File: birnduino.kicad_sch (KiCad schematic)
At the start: 28 parts, among them IC1 ATmega328P, IC2 MAX232, Q1 16 MHz, SW1 RESET, U4 78L33, U5 LM7805

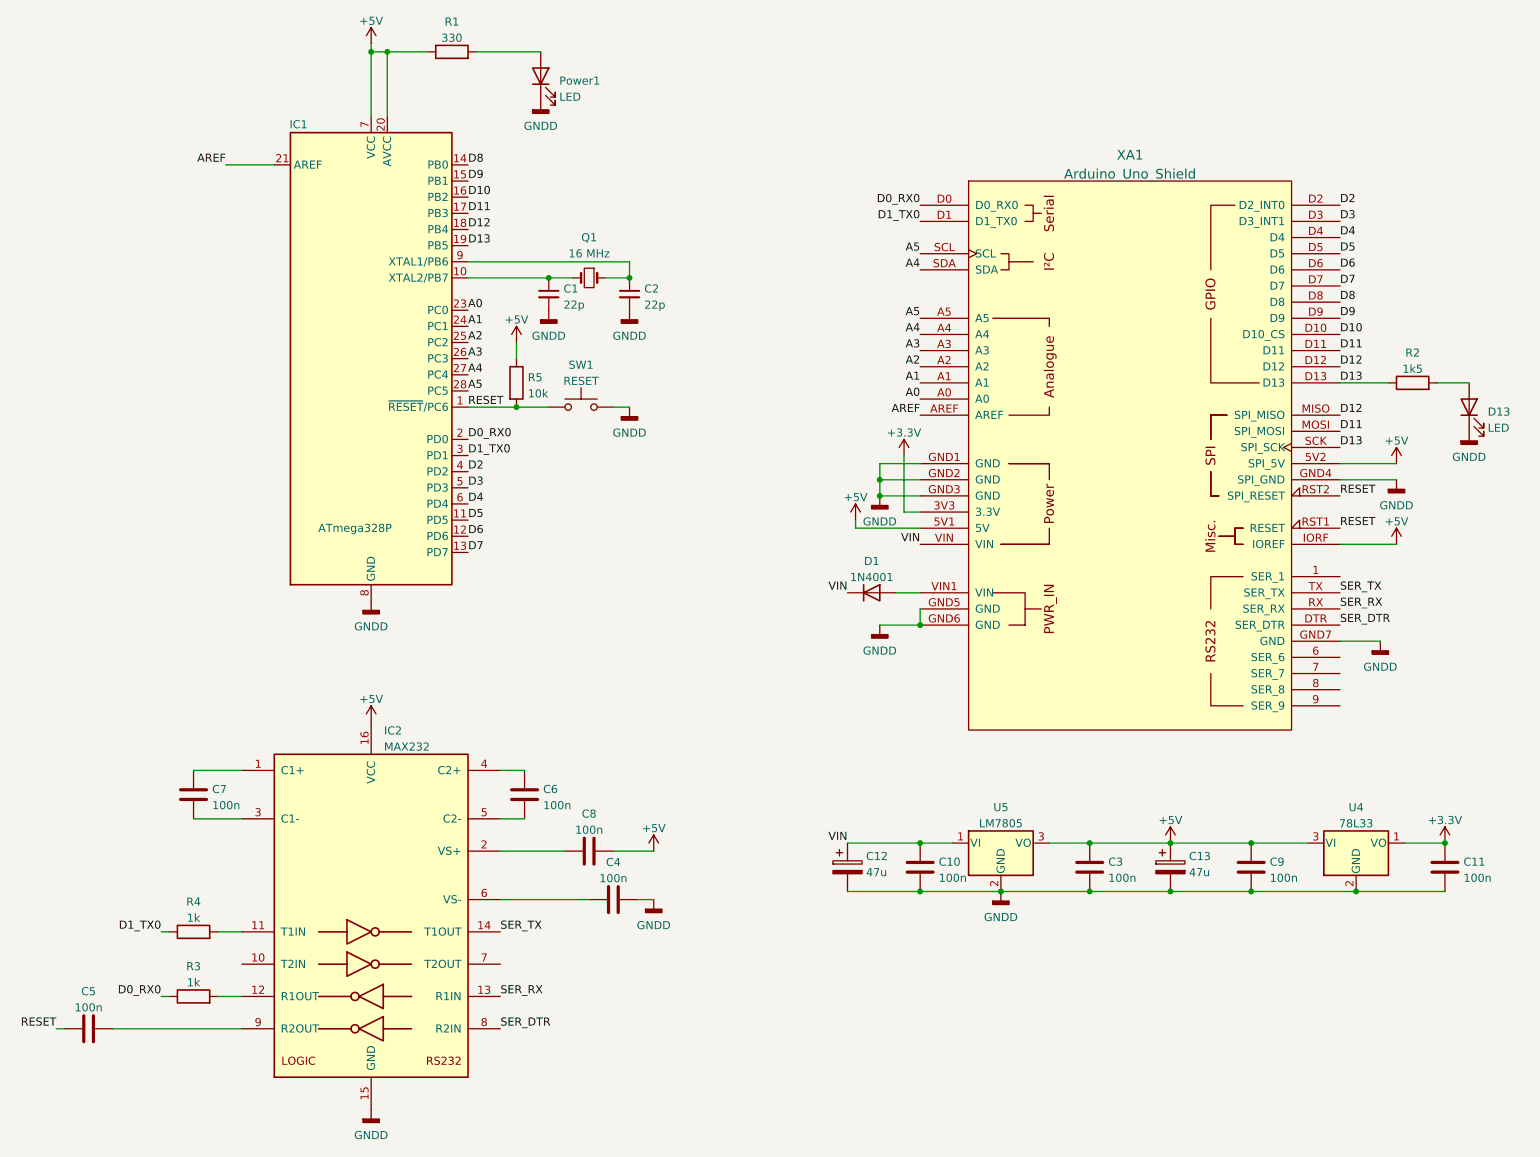
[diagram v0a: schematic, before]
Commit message: Fixed some issues detected by ERC. No impact on board layout.
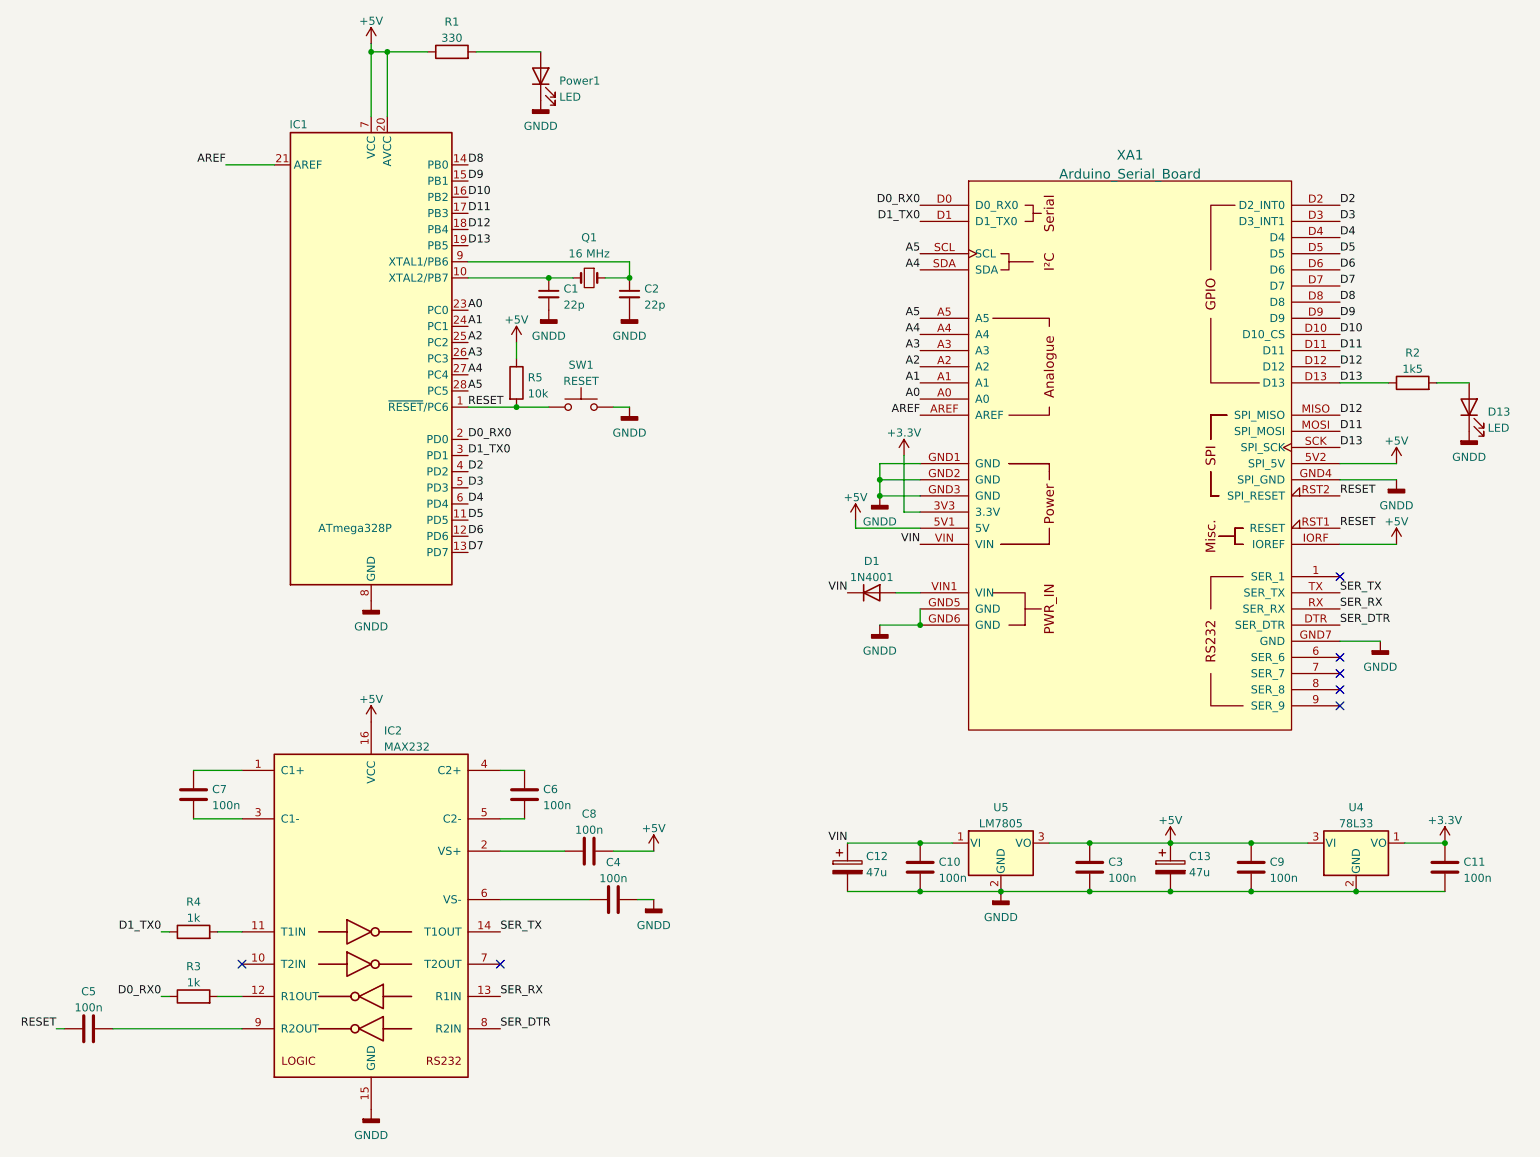
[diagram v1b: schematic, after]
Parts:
- XA1: value Arduino_Uno_Shield -> Arduino_Serial_Board
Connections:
- no-connect marks 0 -> 7
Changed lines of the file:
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@@
   (junction (at 111.76 77.47) (diameter 0) (color 0 0 0 0)
   )
+  (no_connect (at 109.22 165.1))
+  (no_connect (at 68.58 165.1))
+  (no_connect (at 241.3 104.14))
+  (no_connect (at 241.3 119.38))
+  (no_connect (at 241.3 116.84))
+  (no_connect (at 241.3 124.46))
+  (no_connect (at 241.3 121.92))
   (wire (pts (xy 55.88 160.02) (xy 57.15 160.02))
     (stroke (width 0) (type default) (color 0 0 0 0))
@@
       (effects (font (size 1.524 1.524)))
     )
-    (property "Value" "Arduino_Uno_Shield" (id 1) (at 208.28 40.8193 0)
+    (property "Value" "Arduino_Serial_Board" (id 1) (at 208.28 40.8193 0)
       (effects (font (size 1.524 1.524)))
     )
@@
     )
     (path "/d2d8cc72-a089-4a96-b742-afdfb4767d5d"
-      (reference "XA1") (unit 1) (value "Arduino_Uno_Shield") (footprint "Arduino:Arduino_Serial_Shield")
-    )
-  )
+      (reference "XA1") (unit 1) (value "Arduino_Serial_Board") (footprint "Arduino:Arduino_Serial_Shield")
+    )
+  )

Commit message: Update of board/library to change D-SUB connector and power jack.
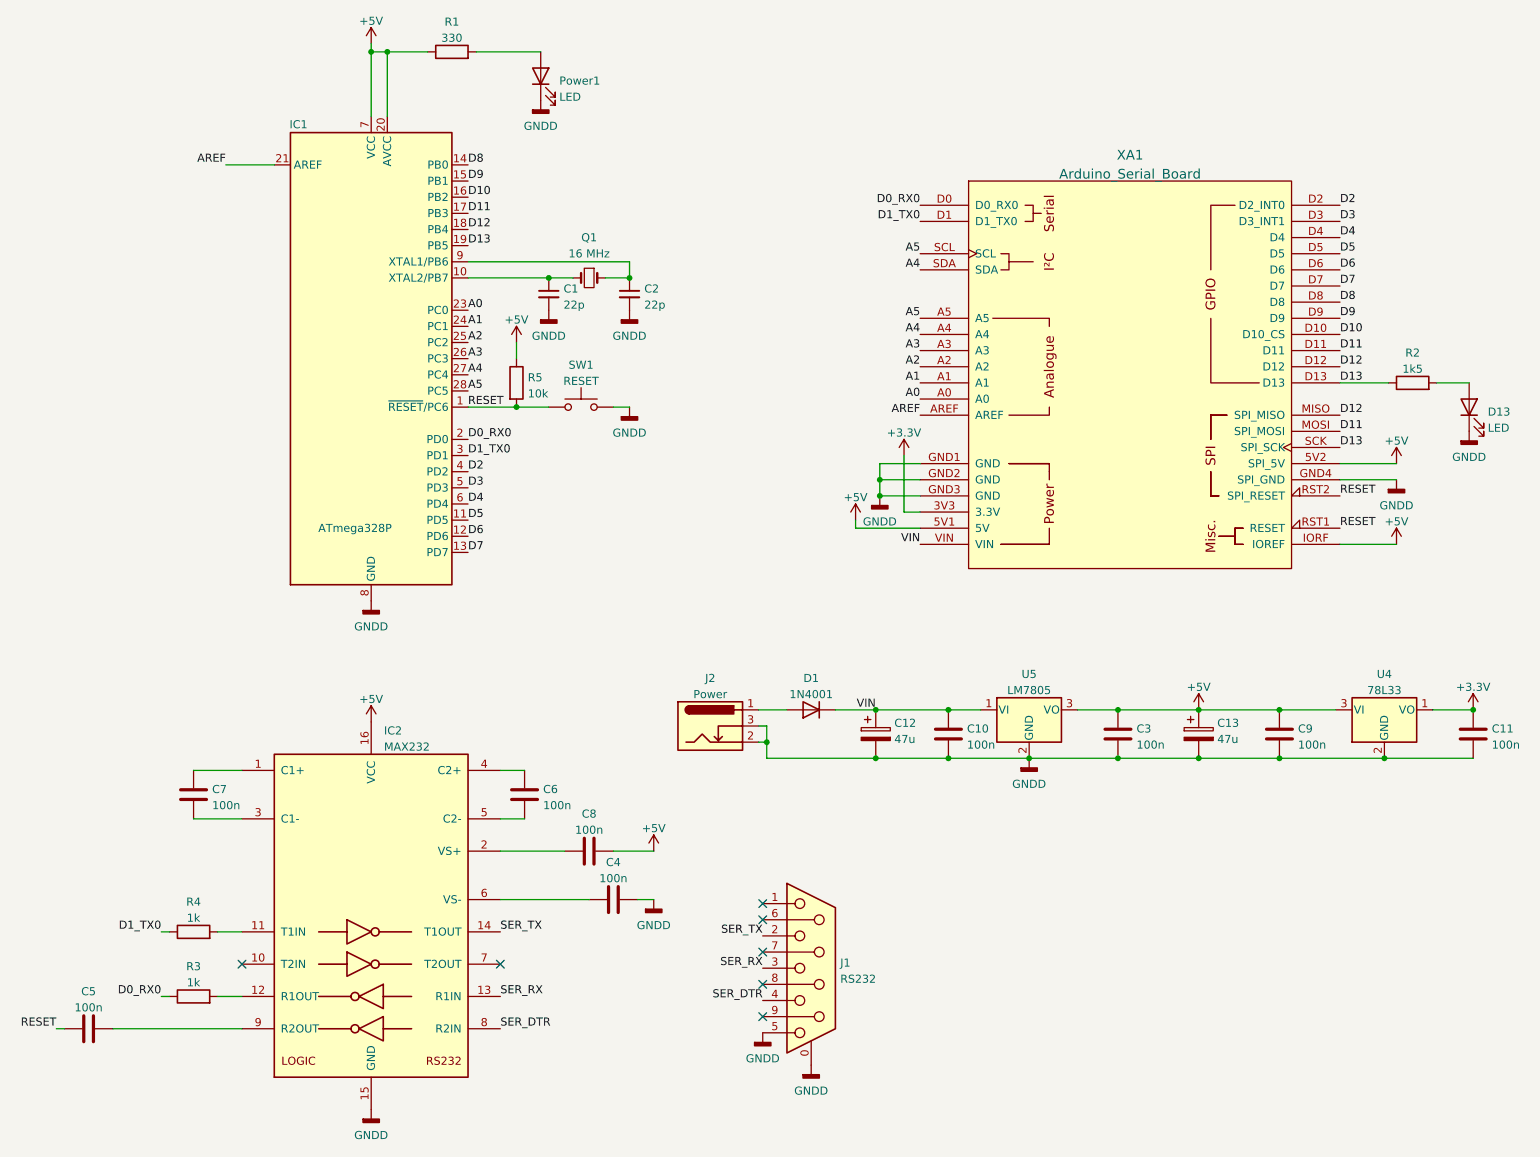
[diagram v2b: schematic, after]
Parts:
- added J1: RS232, Connector_Dsub:DSUB-9_Female_Horizontal_P2.77x2.84mm_EdgePinOffset7.70mm_Housed_MountingHolesOffset9.12mm, symbol Connector:DB9_Female_MountingHoles
- added J2: Power, Connector_BarrelJack:BarrelJack_Horizontal, symbol Connector:Barrel_Jack_Switch
- XA1: symbol arduino:Arduino_Serial_Shield -> arduino:Arduino_Uno_Shield
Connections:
- net GNDD: now also J1.0 (PAD), J1.5, J2.2, J2.3; no longer XA1.GND5 (GND), XA1.GND6 (GND), XA1.GND7 (GND)
- net SER_DTR: now also J1.4; no longer XA1.DTR (SER_DTR)
- net SER_RX: now also J1.3; no longer XA1.RX (SER_RX)
- net SER_TX: now also J1.2; no longer XA1.TX (SER_TX)
- net at D1.2 (A): now also J2.1; no longer XA1.VIN1 (VIN)
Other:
- title: (none) -> Birnduino
- moved on the sheet: C10, C11, C12, C13, C3, C9, D1, U4, U5

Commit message: Removed dependencies to Arduino KiCad Library
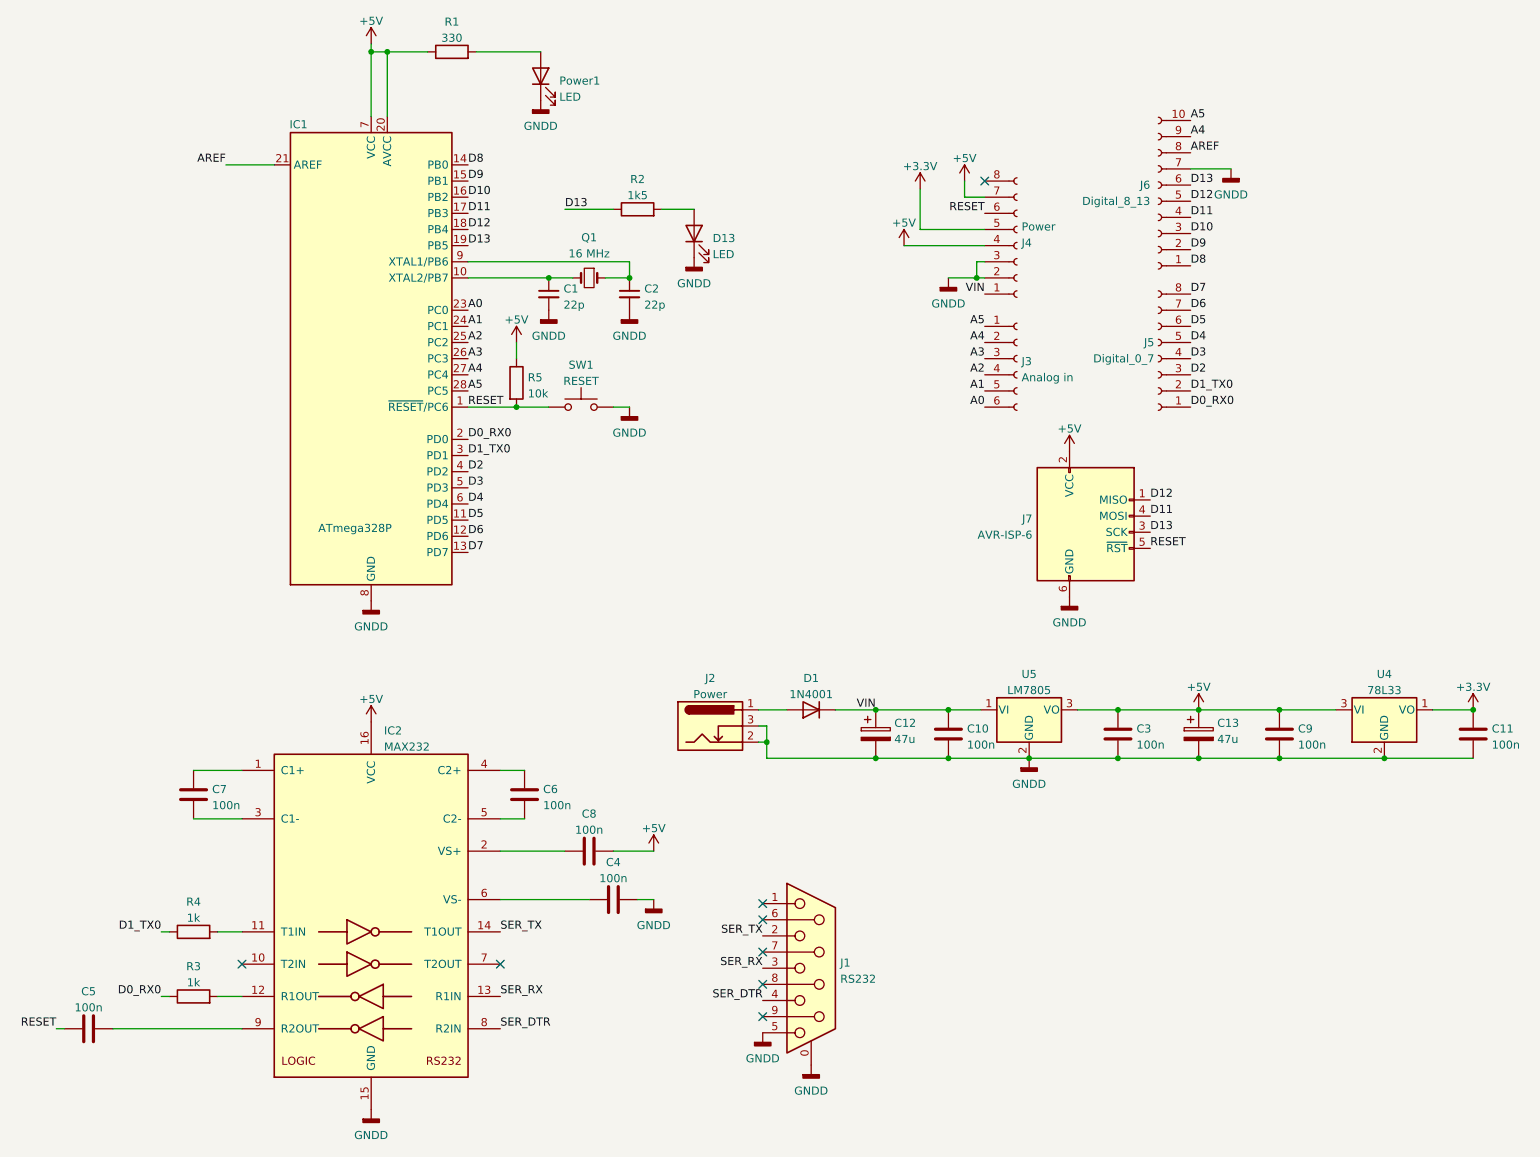
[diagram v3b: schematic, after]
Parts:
- removed XA1: Arduino_Serial_Board, Arduino:Arduino_Serial_Shield, symbol arduino:Arduino_Uno_Shield
- added J3: Analog in, Connector_PinSocket_2.54mm:PinSocket_1x06_P2.54mm_Vertical, symbol Connector:Conn_01x06_Female
- added J4: Power, Connector_PinSocket_2.54mm:PinSocket_1x08_P2.54mm_Vertical, symbol Connector:Conn_01x08_Female
- added J5: Digital_0_7, Connector_PinSocket_2.54mm:PinSocket_1x08_P2.54mm_Vertical, symbol Connector:Conn_01x08_Female
- added J6: Digital_8_13, Connector_PinSocket_2.54mm:PinSocket_1x10_P2.54mm_Vertical, symbol Connector:Conn_01x10_Female
- added J7: AVR-ISP-6, Connector_PinHeader_2.54mm:PinHeader_2x03_P2.54mm_Vertical, symbol Connector:AVR-ISP-6
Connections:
- net +3V3: now also J4.5 (Pin_5)
- net +5V: now also J4.4 (Pin_4), J4.7 (Pin_7), J7.2 (VCC)
- net A0: now also J3.6 (Pin_6)
- net A1: now also J3.5 (Pin_5)
- net A2: now also J3.4 (Pin_4)
- net A3: now also J3.3 (Pin_3)
- net A4: now also J3.2 (Pin_2), J6.9 (Pin_9)
- net A5: now also J3.1 (Pin_1), J6.10 (Pin_10)
- net AREF: now also J6.8 (Pin_8)
- net D0_RX0: now also J5.1 (Pin_1)
- net D10: now also J6.3 (Pin_3)
- net D11: now also J6.4 (Pin_4), J7.4 (MOSI)
- net D12: now also J6.5 (Pin_5), J7.1 (MISO)
- net D13: now also J6.6 (Pin_6), J7.3 (SCK)
- net D1_TX0: now also J5.2 (Pin_2)
- net D2: now also J5.3 (Pin_3)
- net D3: now also J5.4 (Pin_4)
- net D4: now also J5.5 (Pin_5)
- net D5: now also J5.6 (Pin_6)
- net D6: now also J5.7 (Pin_7)
- net D7: now also J5.8 (Pin_8)
- net D8: now also J6.1 (Pin_1)
- net D9: now also J6.2 (Pin_2)
- net GNDD: now also J4.2 (Pin_2), J4.3 (Pin_3), J6.7 (Pin_7), J7.6 (GND)
- net RESET: now also J4.6 (Pin_6), J7.5 (~{RST})
- net VIN: now also J4.1 (Pin_1)
- no-connect marks 7 -> 8
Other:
- moved on the sheet: D13, R2
